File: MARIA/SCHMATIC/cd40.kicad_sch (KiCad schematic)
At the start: 59 parts

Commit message: 3 IN 1
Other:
- note added: "1ST MULTIPLEXER"
- note added: "2ND MULTIPLEXER"
- note added: "ESP8266 BOOTING CIRCUIT"
- note added: "PADS"
- moved on the sheet: J?, R?, U?

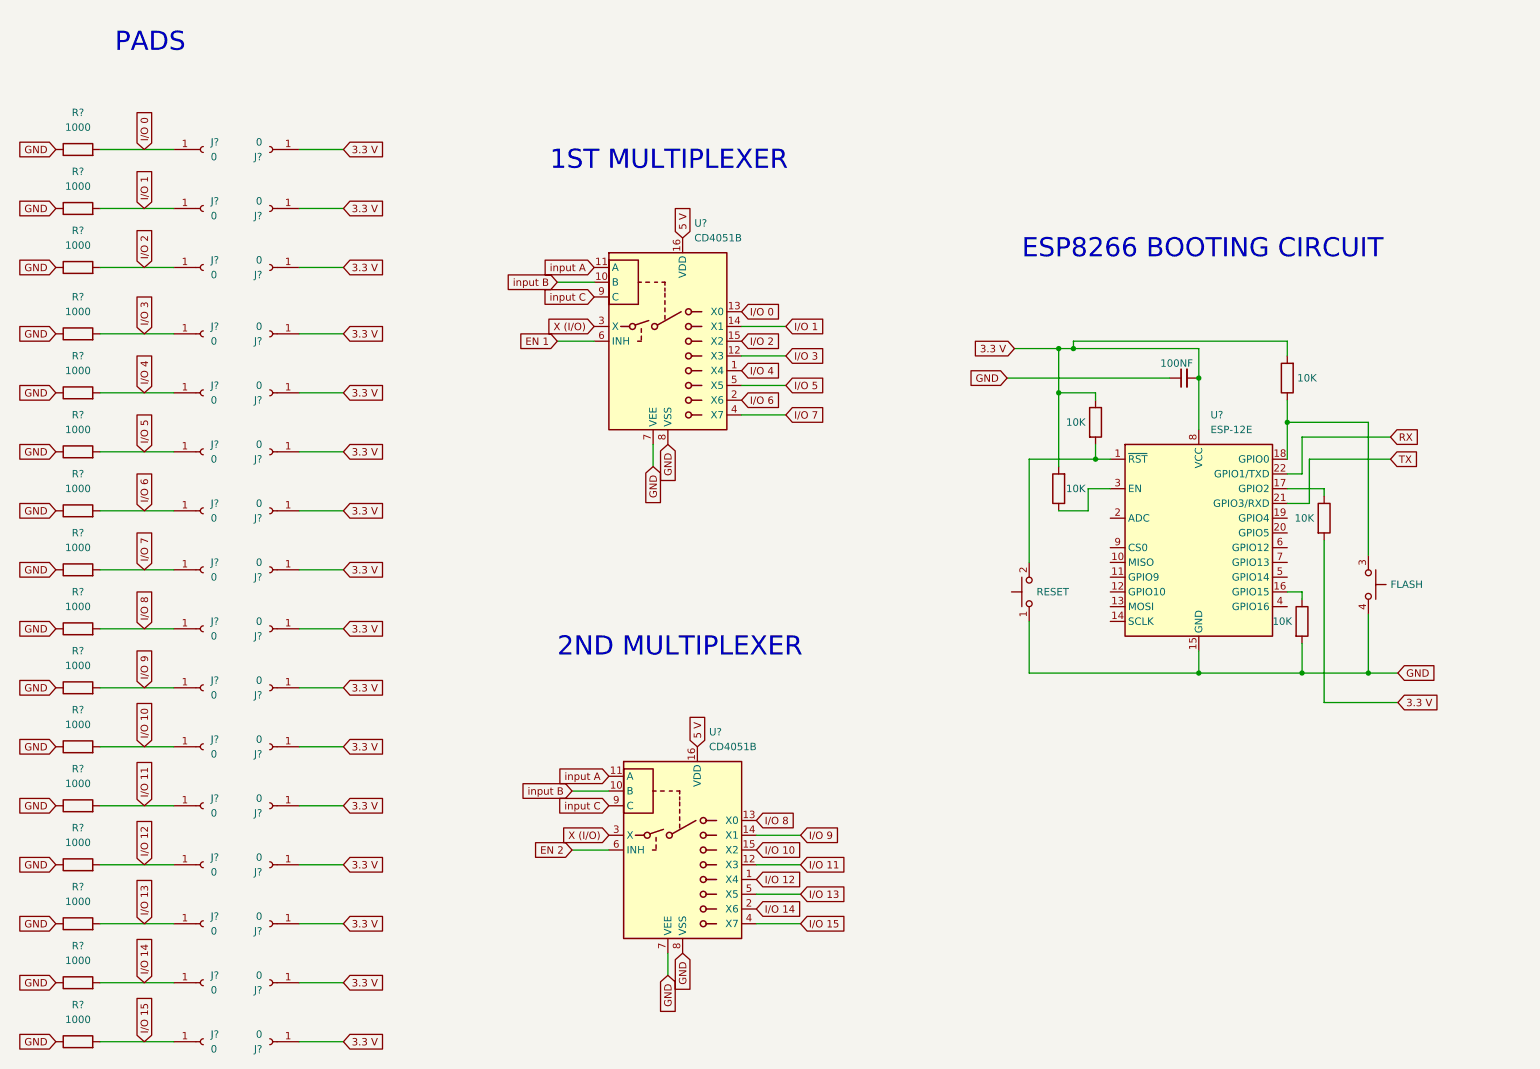
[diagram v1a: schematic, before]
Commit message: CORRECT ERRORS
FTDI CONNECTION FIXED  INTERFACE BOARD CONNECTION CHECK
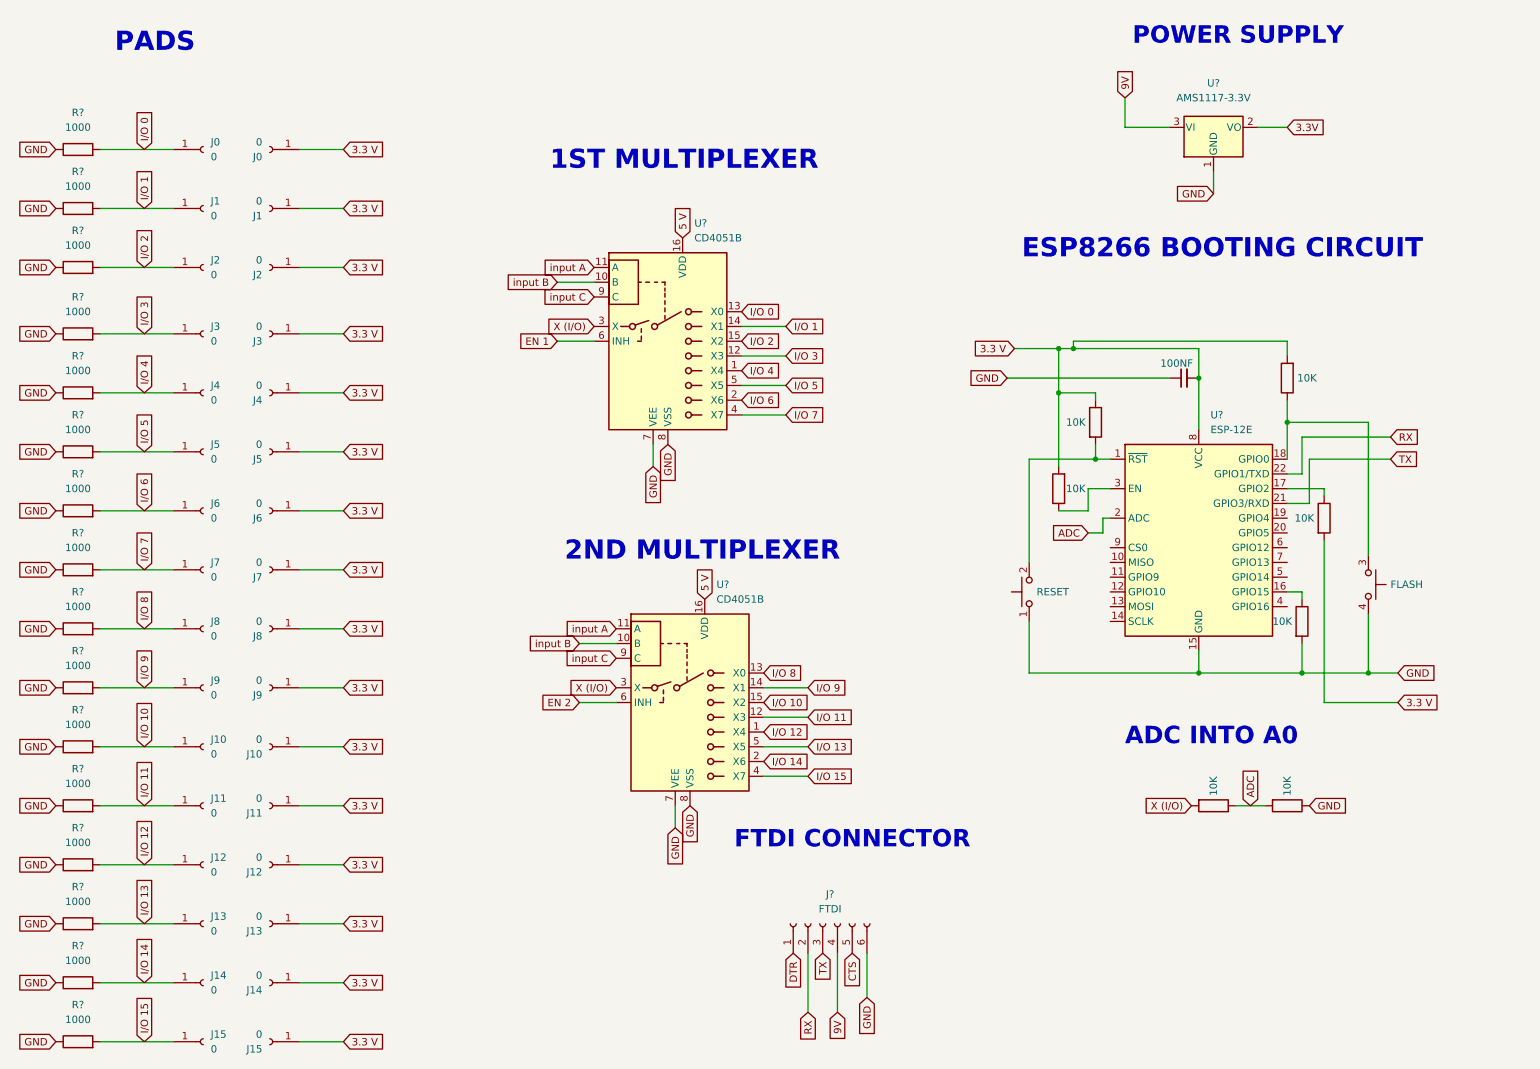
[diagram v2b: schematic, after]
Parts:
- added J?: FTDI, Connector_JST:JST_EH_S6B-EH_1x06_P2.50mm_Horizontal, symbol Connector:Conn_01x06_Female
- added R? (x2): 10K, symbol Device:R
- added U?: AMS1117-3.3V, Package_TO_SOT_SMD:SOT-223-3_TabPin2, symbol Regulator_Linear:AMS1117-3.3
- gave numbers to parts that had none: 16
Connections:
- net GND: now also J?.6 (Pin_6), R?.1, U?.1 (GND)
- net RX: now also J?.2 (Pin_2)
- net TX: now also J?.3 (Pin_3)
- net X (I/O): now also R?.2
- net ADC: now reaches U?.2 (ADC)
- net ADC: now also R?.1, R?.2
- new net 3.3V: U?.2 (VO)
- new net 9V: J?.4 (Pin_4), U?.3 (VI)
- new net CTS: J?.5 (Pin_5)
- new net DTR: J?.1 (Pin_1)
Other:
- note added: "ADC INTO A0"
- note added: "FTDI CONNECTOR"
- note added: "POWER SUPPLY"
- moved on the sheet: U?

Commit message: SCHMETIC COMPLETE FOR INTERFACE BOARD
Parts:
- R?: value 10K -> 200K
- R?: value 10K -> 100K
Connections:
- net 3.3 V: now also R?.1; no longer R?.2
- net EN 1: now also U?.19 (GPIO4)
- net EN 2: now also U?.20 (GPIO5)
- net input A: now also U?.5 (GPIO14)
- net input B: now also U?.6 (GPIO12)
- net input C: now also U?.7 (GPIO13)
- net at U?.17 (GPIO2): now also R?.2; no longer R?.1
- net 9V renamed 5V
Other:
- moved on the sheet: J?, U?

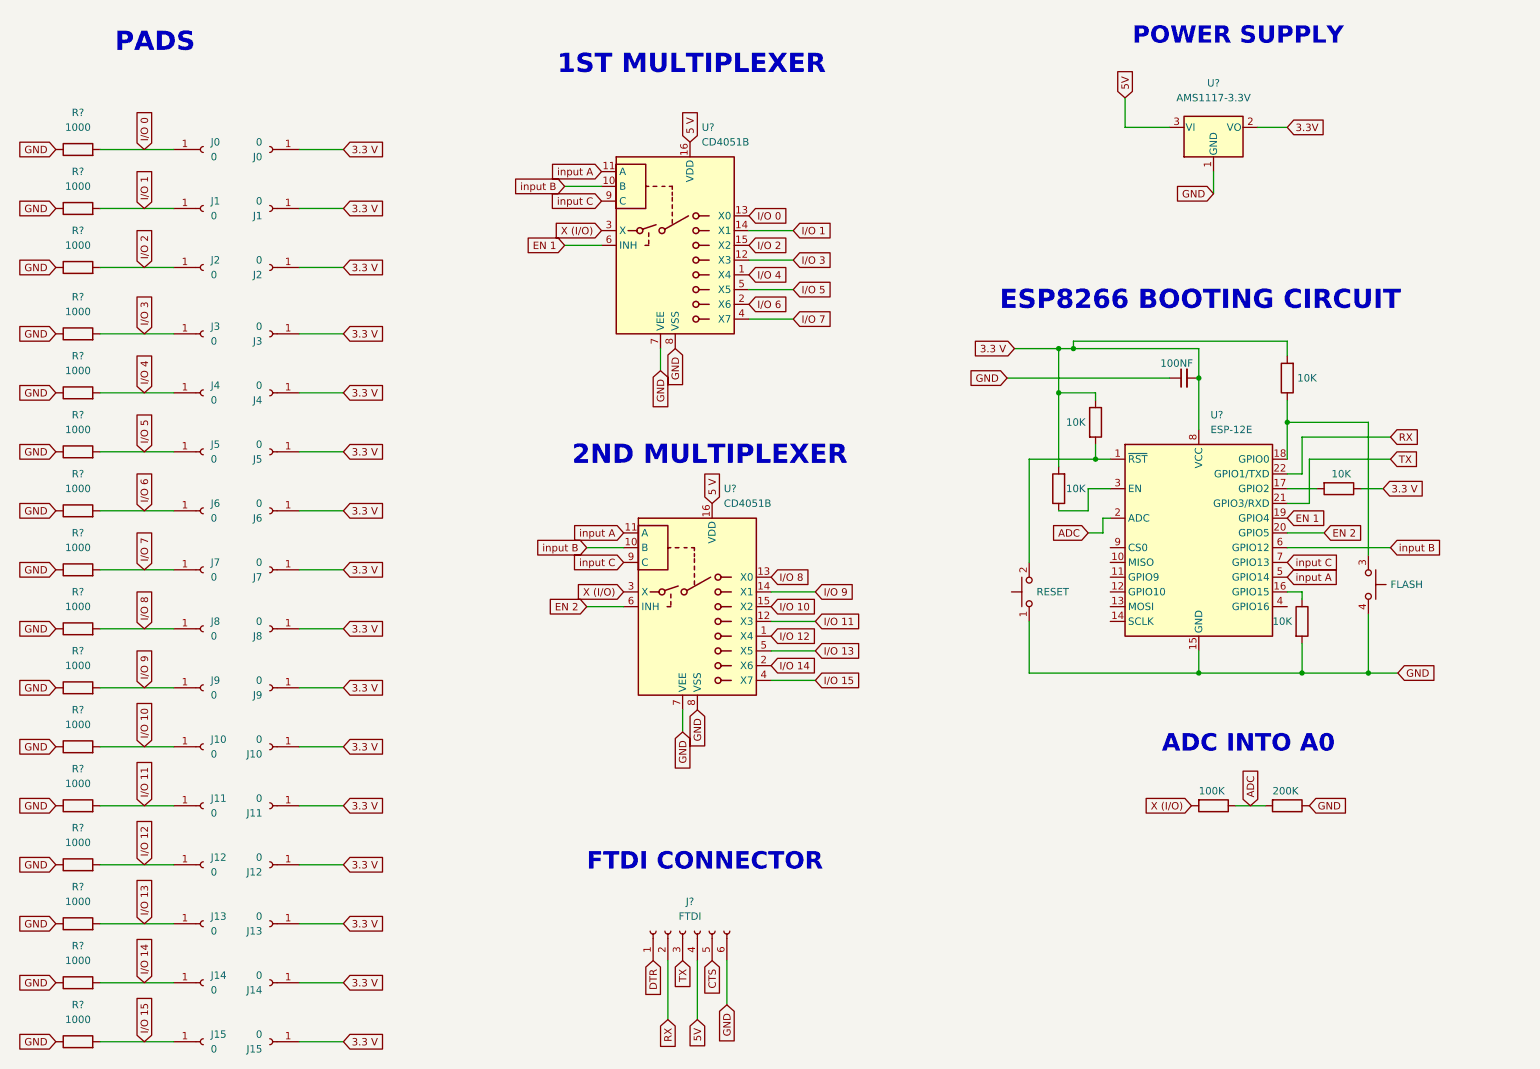
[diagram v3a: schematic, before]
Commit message: HEADING ADDED
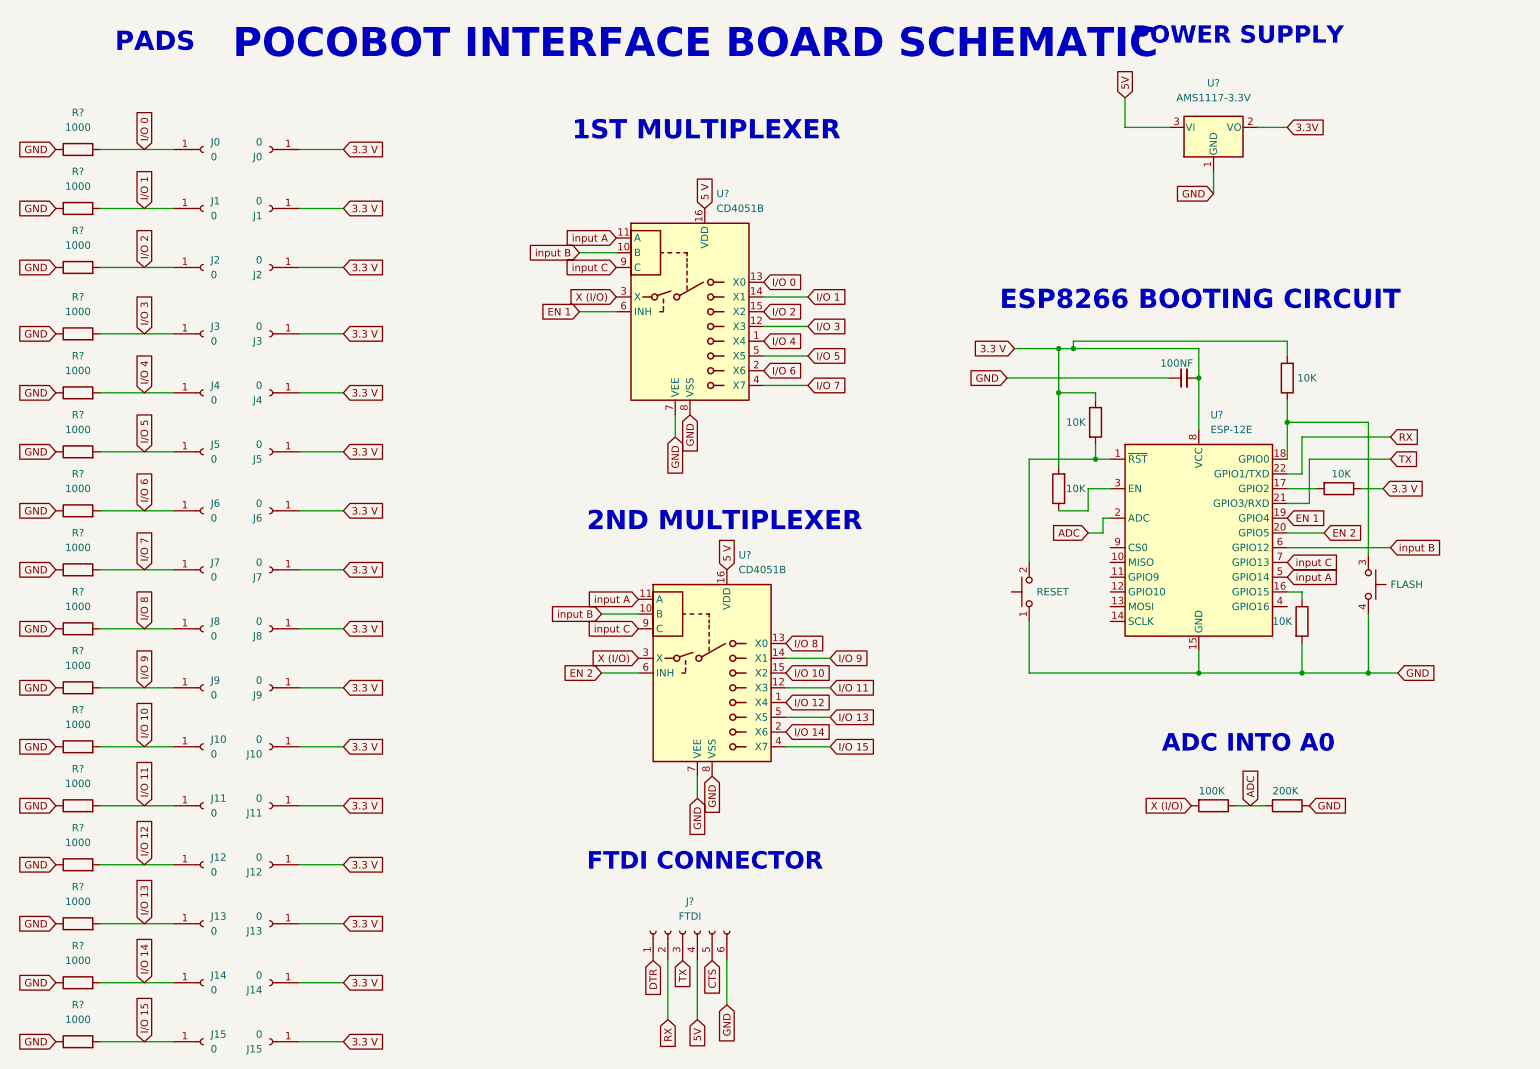
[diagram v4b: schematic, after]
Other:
- note added: "POCOBOT INTERFACE BOARD SCHEMATIC"
- moved on the sheet: U?
